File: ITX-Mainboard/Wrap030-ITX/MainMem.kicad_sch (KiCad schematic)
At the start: 28 parts, among them U2 TE-822021-4, U4 74HC245, U5 74HC245, U6 74HC245, U7 74HC245, U8 TE-822021-4

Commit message: Schematic substantial completion
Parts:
- C1: footprint Capacitor_SMD:C_0805_2012Metric -> Capacitor_SMD:C_0402_1005Metric_Pad0.74x0.62mm_HandSolder; JLC-Part (none) -> https://jlcpcb.com/partdetail/1877-CL05B104KO5NNNC/C1525
- C15: footprint Capacitor_SMD:C_0805_2012Metric -> Capacitor_SMD:C_0402_1005Metric_Pad0.74x0.62mm_HandSolder; JLC-Part (none) -> https://jlcpcb.com/partdetail/53938-CL05A105KA5NQNC/C52923
- RN1: Mouser-Part (none) -> 603-YC124-JR-1033RL; Notes (none) -> 33R x4
- U4, U5, U6, U7: footprint (none) -> Package_DIP:DIP-20_W7.62mm_Socket

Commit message: PCB substantial completion
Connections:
- net FC0 is gone; now on net MEM-A0: VGEN1.12 (IO3)
- net FC1 is gone; now on net CPU-A2: VGEN1.11 (IO5)
- net FC2 is gone; now on net CPU-A3: VGEN1.10 (IO6)
- net CPU-A0: now also VGEN1.51 (IO77); no longer VGEN1.44 (IO65)
- net CPU-A1: now also VGEN1.54 (IO83); no longer VGEN1.45 (IO67)
- net CPU-A10: now also VGEN1.79 (IO125); no longer VGEN1.56 (IO86)
- net CPU-A11: now also VGEN1.77 (IO123); no longer VGEN1.57 (IO88)
- net CPU-A12: now also VGEN1.75 (IO118); no longer VGEN1.58 (IO91)
- net CPU-A13: now also VGEN1.76 (IO120); no longer VGEN1.60 (IO93)
- net CPU-A14: now also VGEN1.74 (IO117); no longer VGEN1.61 (IO94)
- net CPU-A15: now also VGEN1.73 (IO115); no longer VGEN1.63 (IO97)
- net CPU-A16: now also VGEN1.69 (IO107); no longer VGEN1.64 (IO99)
- net CPU-A17: now also VGEN1.70 (IO109); no longer VGEN1.65 (IO101)
- net CPU-A2: no longer VGEN1.46 (IO69)
- net CPU-A20: now also VGEN1.64 (IO99); no longer VGEN1.69 (IO107)
- net CPU-A21: now also VGEN1.65 (IO101); no longer VGEN1.70 (IO109)
- net CPU-A22: now also VGEN1.63 (IO97); no longer VGEN1.73 (IO115)
- net CPU-A23: now also VGEN1.60 (IO93); no longer VGEN1.74 (IO117)
- net CPU-A24: now also VGEN1.58 (IO91); no longer VGEN1.75 (IO118)
- net CPU-A25: now also VGEN1.61 (IO94); no longer VGEN1.76 (IO120)
- net CPU-A26: now also VGEN1.57 (IO88); no longer VGEN1.77 (IO123)
- net CPU-A27: now also VGEN1.56 (IO86); no longer VGEN1.79 (IO125)
- net CPU-A28: now also VGEN1.52 (IO80); no longer VGEN1.80 (IO126)
- net CPU-A29: now also VGEN1.55 (IO85); no longer VGEN1.81 (IO128)
- net CPU-A3: no longer VGEN1.48 (IO72)
- net CPU-A4: now also VGEN1.8 (IO11); no longer VGEN1.49 (IO73)
- net CPU-A5: now also VGEN1.6 (IO13); no longer VGEN1.50 (IO75)
- net CPU-A6: now also VGEN1.9 (IO8); no longer VGEN1.51 (IO77)
- net CPU-A7: now also VGEN1.4 (IO16); no longer VGEN1.52 (IO80)
- net CPU-A8: now also VGEN1.80 (IO126); no longer VGEN1.54 (IO83)
- net CPU-A9: now also VGEN1.5 (IO14); no longer VGEN1.55 (IO85)
- net CPU-D0: now also U7.11 (B7); no longer U4.18 (B0)
- net CPU-D1: now also U7.12 (B6); no longer U4.17 (B1)
- net CPU-D10: now also U5.13 (B5); no longer U5.16 (B2)
- net CPU-D11: now also U5.14 (B4); no longer U5.15 (B3)
- net CPU-D12: now also U5.15 (B3); no longer U5.14 (B4)
- net CPU-D13: now also U5.16 (B2); no longer U5.13 (B5)
- net CPU-D14: now also U5.17 (B1); no longer U5.12 (B6)
- net CPU-D15: now also U5.18 (B0); no longer U5.11 (B7)
- net CPU-D16: now also U4.11 (B7); no longer U6.18 (B0)
- net CPU-D17: now also U4.12 (B6); no longer U6.17 (B1)
- net CPU-D18: now also U4.13 (B5); no longer U6.16 (B2)
- net CPU-D19: now also U4.14 (B4); no longer U6.15 (B3)
- net CPU-D2: now also U7.13 (B5); no longer U4.16 (B2)
- net CPU-D20: now also U4.15 (B3); no longer U6.14 (B4)
- net CPU-D21: now also U4.16 (B2); no longer U6.13 (B5)
- net CPU-D22: now also U4.17 (B1); no longer U6.12 (B6)
- net CPU-D23: now also U4.18 (B0); no longer U6.11 (B7)
- net CPU-D24: now also U6.11 (B7); no longer U7.18 (B0)
- net CPU-D25: now also U6.12 (B6); no longer U7.17 (B1)
- net CPU-D26: now also U6.13 (B5); no longer U7.16 (B2)
- net CPU-D27: now also U6.14 (B4); no longer U7.15 (B3)
- net CPU-D28: now also U6.15 (B3); no longer U7.14 (B4)
- net CPU-D29: now also U6.16 (B2); no longer U7.13 (B5)
- net CPU-D3: now also U7.14 (B4); no longer U4.15 (B3)
- net CPU-D30: now also U6.17 (B1); no longer U7.12 (B6)
- net CPU-D31: now also U6.18 (B0); no longer U7.11 (B7)
- net CPU-D4: now also U7.15 (B3); no longer U4.14 (B4)
- net CPU-D5: now also U7.16 (B2); no longer U4.13 (B5)
- net CPU-D6: now also U7.17 (B1); no longer U4.12 (B6)
- net CPU-D7: now also U7.18 (B0); no longer U4.11 (B7)
- net CPU-D8: now also U5.11 (B7); no longer U5.18 (B0)
- net CPU-D9: now also U5.12 (B6); no longer U5.17 (B1)
- net MEM-A0: no longer VGEN1.4 (IO16)
- net MEM-A1: now also VGEN1.15 (IO29); no longer VGEN1.22 (IO17)
- net MEM-A10: now also RN1.4 (R4.1), VGEN1.22 (IO17); no longer RN1.3 (R3.1), VGEN1.29 (IO38)
- net MEM-A10R: now also RN1.5 (R4.2); no longer RN1.6 (R3.2)
- net MEM-A11: now also RN1.2 (R2.1), VGEN1.25 (IO45); no longer RN1.4 (R4.1), VGEN1.28 (IO40)
- net MEM-A11R: now also RN1.7 (R2.2); no longer RN1.5 (R4.2)
- net MEM-A2: now also VGEN1.17 (IO25); no longer VGEN1.21 (IO19)
- net MEM-A3: now also VGEN1.16 (IO27); no longer VGEN1.20 (IO21)
- net MEM-A5: now also VGEN1.21 (IO19); no longer VGEN1.17 (IO25)
- net MEM-A6: now also VGEN1.20 (IO21); no longer VGEN1.16 (IO27)
- net MEM-A7: now also RN1.1 (R1.1), VGEN1.24 (IO46); no longer RN1.4 (R4.1), VGEN1.15 (IO29)
- net MEM-A7R: now also RN1.8 (R1.2); no longer RN1.5 (R4.2)
- net MEM-A8: now also RN1.3 (R3.1), VGEN1.27 (IO43); no longer RN1.1 (R1.1), VGEN1.31 (IO35)
- net MEM-A8R: now also RN1.6 (R3.2); no longer RN1.8 (R1.2)
- net MEM-A9: now also RN1.4 (R4.1), VGEN1.28 (IO40); no longer RN1.2 (R2.1), VGEN1.30 (IO37)
- net MEM-A9R: now also RN1.5 (R4.2); no longer RN1.7 (R2.2)
- net R/~{W}: now also VGEN1.81 (IO128); no longer VGEN1.5 (IO14)
- net SIZ0: now also VGEN1.48 (IO72); no longer VGEN1.9 (IO8)
- net SIZ1: now also VGEN1.49 (IO73); no longer VGEN1.8 (IO11)
- net ~{AS}: now also VGEN1.50 (IO75); no longer VGEN1.6 (IO13)
- net ~{MEM-CAS0}: now also RN1.3 (R3.1), VGEN1.35 (IO59); no longer RN1.1 (R1.1), VGEN1.40 (IO51)
- net ~{MEM-CAS1R}: now also RN1.5 (R4.2); no longer RN1.7 (R2.2)
- net ~{MEM-CAS1}: now also RN1.4 (R4.1), VGEN1.37 (IO56); no longer RN1.2 (R2.1), VGEN1.39 (IO53)
- net ~{MEM-CAS2R}: now also RN1.7 (R2.2); no longer RN1.6 (R3.2)
- net ~{MEM-CAS2}: now also RN1.1 (R1.1), VGEN1.33 (IO64); no longer RN1.3 (R3.1), VGEN1.37 (IO56)
- net ~{MEM-CAS3R}: now also RN1.6 (R3.2); no longer RN1.5 (R4.2)
- net ~{MEM-CAS3}: now also RN1.2 (R2.1); no longer RN1.4 (R4.1)
- net ~{MEM-RAS0R}: now also RN1.5 (R4.2); no longer RN1.8 (R1.2)
- net ~{MEM-RAS0}: now also RN1.4 (R4.1), VGEN1.34 (IO61); no longer RN1.1 (R1.1), VGEN1.27 (IO43)
- net ~{MEM-RAS1R}: now also RN1.6 (R3.2); no longer RN1.7 (R2.2)
- net ~{MEM-RAS1}: now also RN1.3 (R3.1), VGEN1.31 (IO35); no longer RN1.2 (R2.1), VGEN1.25 (IO45)
- net ~{MEM-RAS2R}: now also RN1.7 (R2.2); no longer RN1.6 (R3.2)
- net ~{MEM-RAS2}: now also RN1.2 (R2.1), VGEN1.30 (IO37); no longer RN1.3 (R3.1), VGEN1.24 (IO46)
- net ~{MEM-RAS3R}: now also RN1.8 (R1.2); no longer RN1.5 (R4.2)
- net ~{MEM-RAS3}: now also RN1.1 (R1.1), VGEN1.29 (IO38); no longer RN1.4 (R4.1), VGEN1.41 (IO49)
- net ~{MEM-WE}: now also VGEN1.40 (IO51); no longer VGEN1.35 (IO59)
- net ~{RAM-DSACK}: now also VGEN1.39 (IO53); no longer VGEN1.33 (IO64)

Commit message: Completing PCB Routing
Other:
- title: Wrap030 ITX -> Wrap030-ATX Mainboard
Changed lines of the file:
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@@
   (paper "USLetter")
   (title_block
-    (title "Wrap030 ITX")
-    (date "2023-03-15")
-    (rev "0")
+    (title "Wrap030-ATX Mainboard")
+    (date "2023-03-26")
+    (rev "1")
     (company "techav")
   )

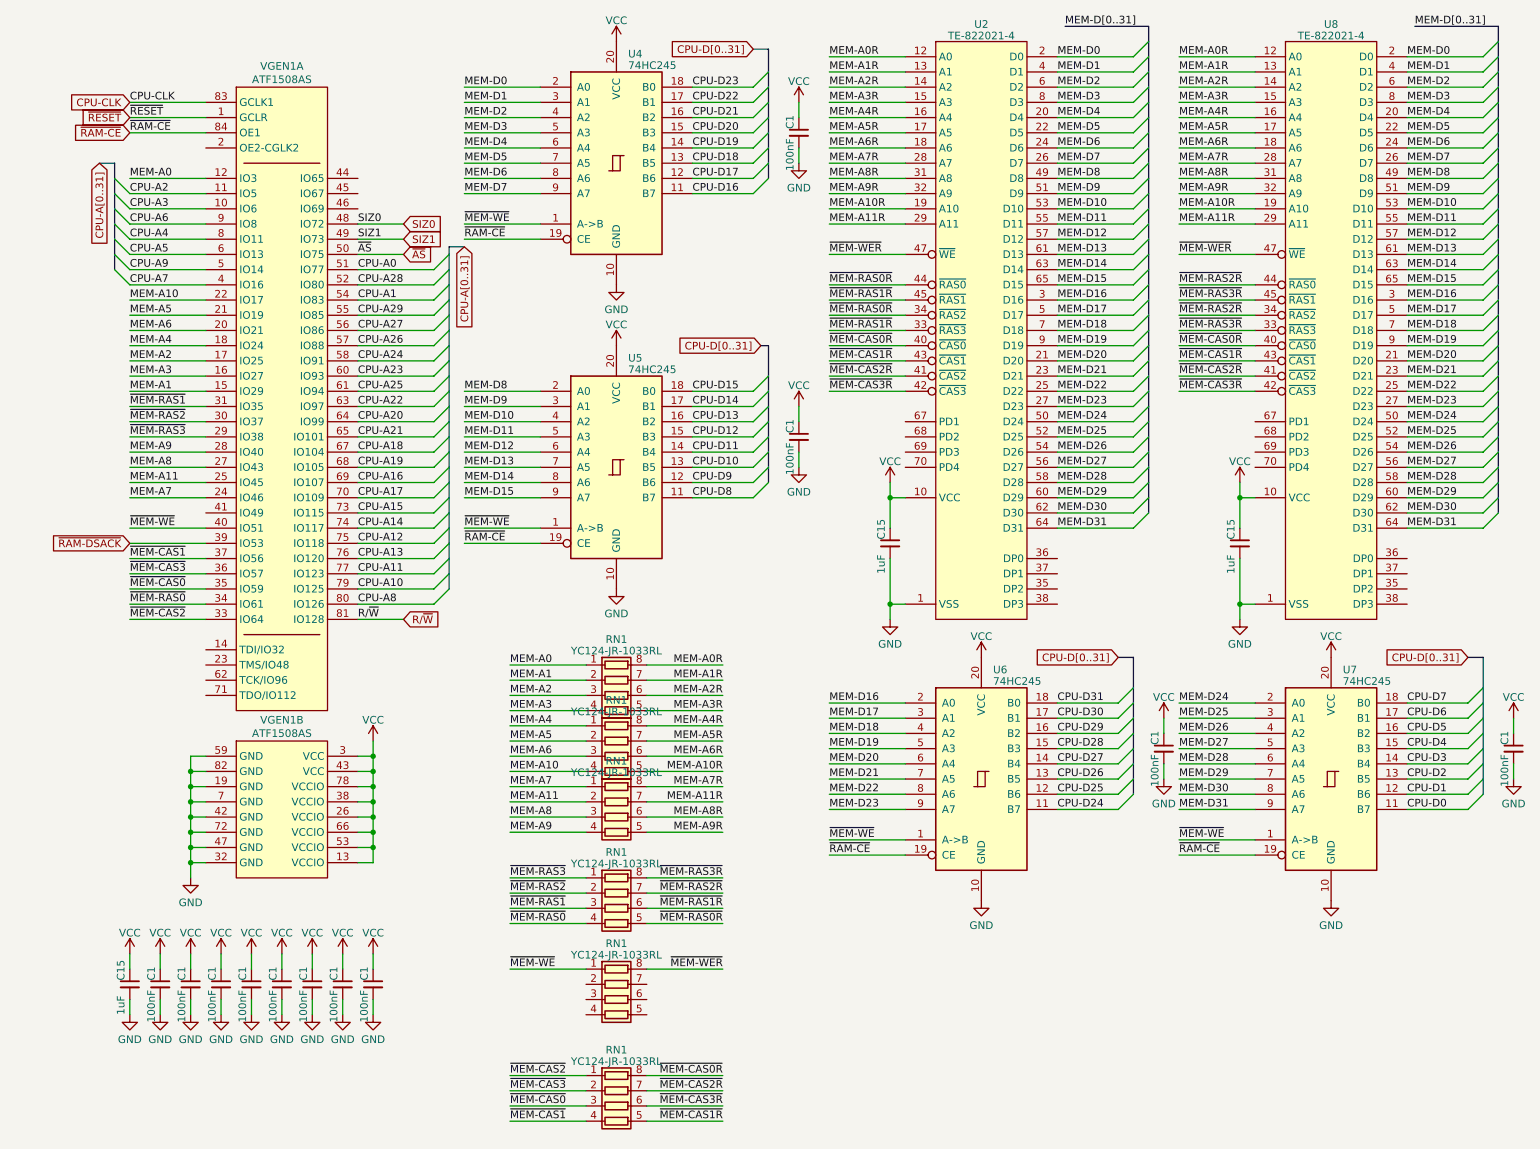
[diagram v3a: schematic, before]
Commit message: PCB Silkscreen & DRC Cleanup
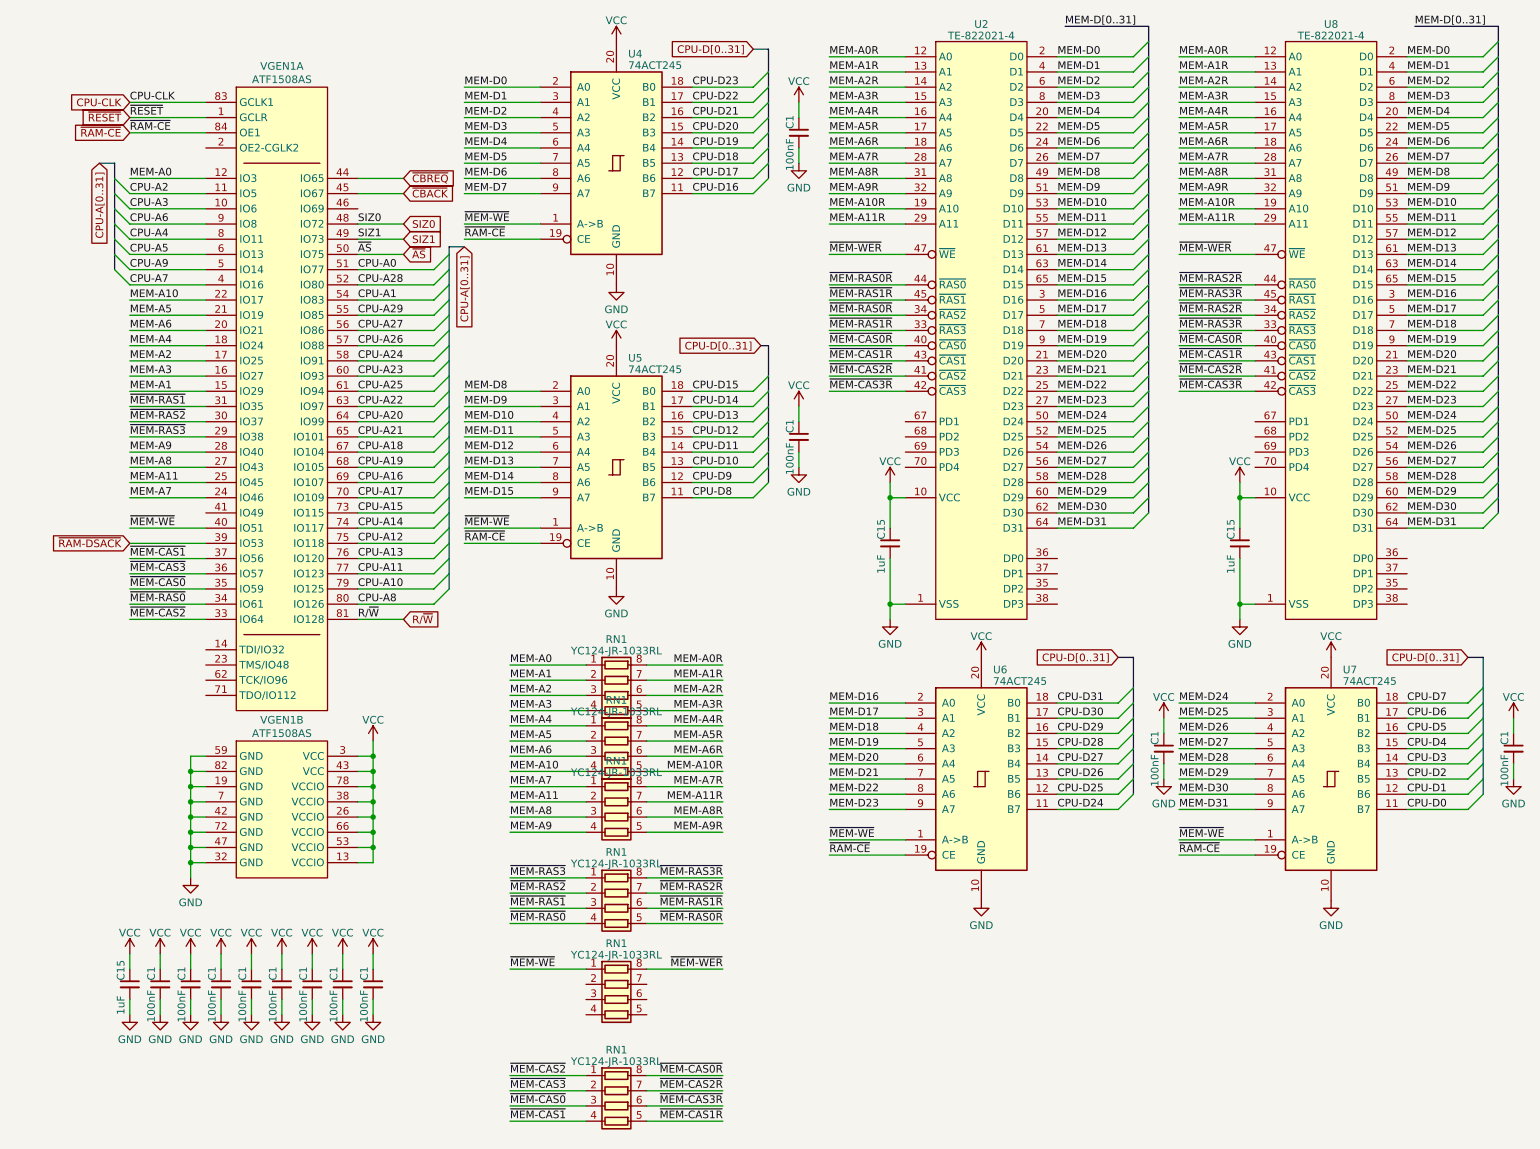
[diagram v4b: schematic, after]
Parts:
- U4, U5, U6, U7: value 74HC245 -> 74ACT245
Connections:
- net ~{CBREQ}: now reaches VGEN1.44 (IO65)
- net ~{CBACK}: now reaches VGEN1.45 (IO67)
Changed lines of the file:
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@@
     (stroke (width 0) (type default))
   )
+  (wire (pts (xy 71.12 43.18) (xy 63.5 43.18))
+    (stroke (width 0) (type default))
+  )
   (bus (pts (xy 195.58 17.78) (xy 195.58 20.32))
     (stroke (width 0) (type default))
@@
     (stroke (width 0) (type default))
   )
+  (wire (pts (xy 71.12 40.64) (xy 63.5 40.64))
+    (stroke (width 0) (type default))
+  )
   (wire (pts (xy 200.66 48.26) (xy 213.36 48.26))
     (stroke (width 0) (type default))
@@
     )
   )
+  (global_label "~{CBREQ}" (shape input) (at 71.12 40.64 0) (fields_autoplaced)
+    (effects (font (size 1.27 1.27)) (justify left))
+    (property "Intersheetrefs" "${INTERSHEET_REFS}" (at 80.3153 40.64 0)
+      (effects (font (size 1.27 1.27)) (justify left) hide)
+    )
+  )
   (global_label "SIZ1" (shape input) (at 71.12 50.8 0) (fields_autoplaced)
     (effects (font (size 1.27 1.27)) (justify left))
@@
     )
   )
+  (global_label "~{CBACK}" (shape input) (at 71.12 43.18 0) (fields_autoplaced)
+    (effects (font (size 1.27 1.27)) (justify left))
+    (property "Intersheetrefs" "${INTERSHEET_REFS}" (at 80.1944 43.18 0)
+      (effects (font (size 1.27 1.27)) (justify left) hide)
+    )
+  )
   (global_label "CPU-D[0..31]" (shape input) (at 130.81 68.58 180) (fields_autoplaced)
     (effects (font (size 1.27 1.27)) (justify right))
@@
       (effects (font (size 1.27 1.27)) (justify left))
     )
-    (property "Value" "74HC245" (at 108.6359 72.5711 0)
+    (property "Value" "74ACT245" (at 108.6359 72.5711 0)
       (effects (font (size 1.27 1.27)) (justify left))
     )
@@
       (effects (font (size 1.27 1.27)) (justify left))
     )
-    (property "Value" "74HC245" (at 228.0159 124.6411 0)
+    (property "Value" "74ACT245" (at 228.0159 124.6411 0)
       (effects (font (size 1.27 1.27)) (justify left))
     )
@@
       (effects (font (size 1.27 1.27)) (justify left))
     )
-    (property "Value" "74HC245" (at 169.5959 124.6411 0)
+    (property "Value" "74ACT245" (at 169.5959 124.6411 0)
       (effects (font (size 1.27 1.27)) (justify left))
     )
@@
       (effects (font (size 1.27 1.27)) (justify left))
     )
-    (property "Value" "74HC245" (at 108.6359 21.7711 0)
+    (property "Value" "74ACT245" (at 108.6359 21.7711 0)
       (effects (font (size 1.27 1.27)) (justify left))
     )

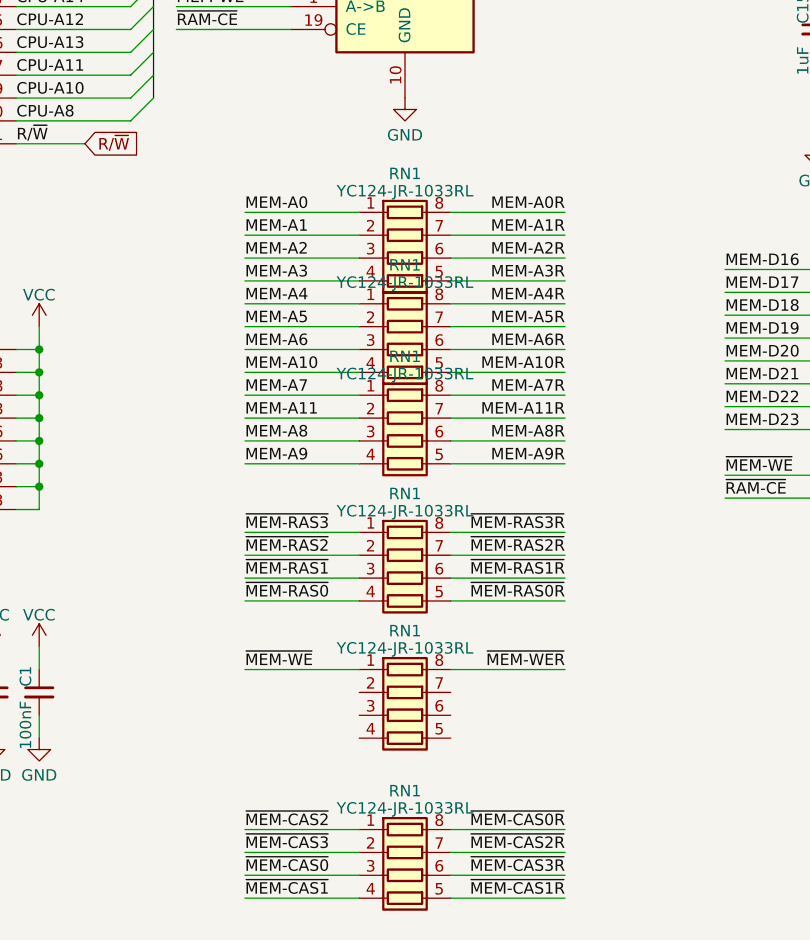
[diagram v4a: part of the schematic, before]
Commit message: Replace resistor nets with 0402 & update gerbers
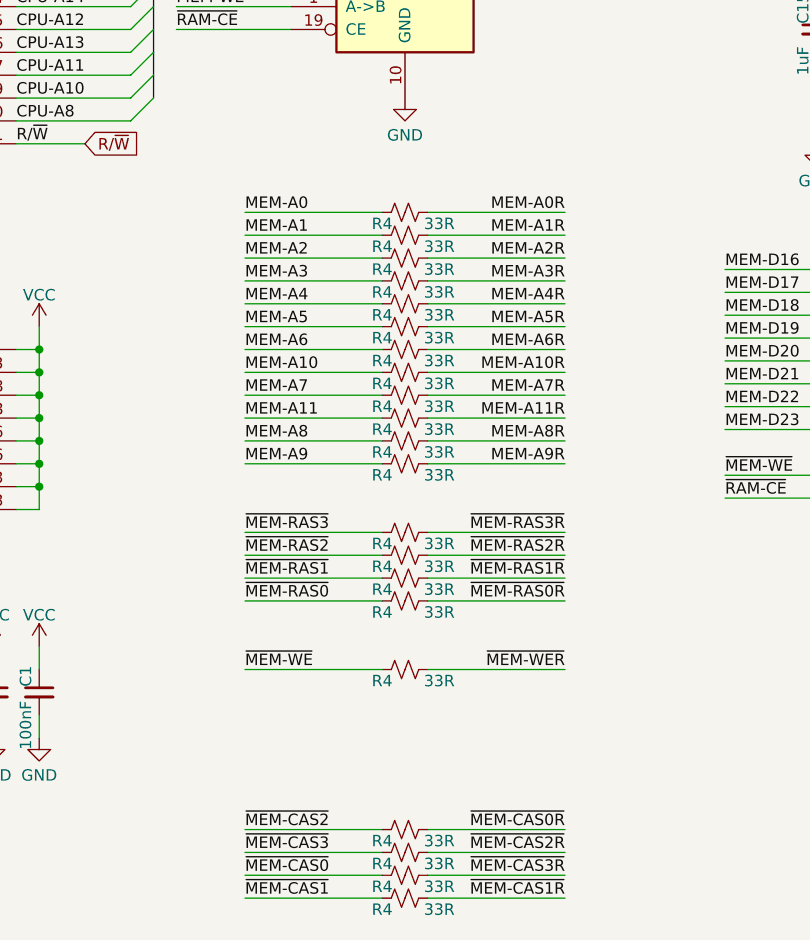
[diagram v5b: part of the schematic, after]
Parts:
- removed RN1 (x6): YC124-JR-1033RL, Resistor_SMD:R_Array_Convex_4x1206, symbol Device:R_Pack04
- added R4 (x21): 33R, Resistor_SMD:R_0603_1608Metric_Pad0.98x0.95mm_HandSolder, symbol Device:R_Small_US
- C1: Mouser-Part (none) -> 187-CL05B104KO5NNNC; Notes (none) -> JLC
- C15: Mouser-Part (none) -> 187-CL05A105KA5NQNC; Notes (none) -> JLC
- U2, U8: Mouser-Part (none) -> 571-5822021-4; Notes (none) -> OFE
- U4, U5, U6, U7: Mouser-Part (none) -> 595-SN74ACT245N; Notes (none) -> OFE; Socket-Mouser (none) -> 571-1-2199298-6
- VGEN1: Mouser-Part (none) -> 556-ATF1508AS-10JU84; Notes (none) -> OFE; Socket-Mouser (none) -> 575-948424
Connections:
- net MEM-A0: now also R4.1
- net MEM-A0R: now also R4.2
- net MEM-A1: now also R4.1
- net MEM-A10: now also R4.1
- net MEM-A10R: now also R4.2
- net MEM-A11: now also R4.1
- net MEM-A11R: now also R4.2
- net MEM-A1R: now also R4.2
- net MEM-A2: now also R4.1
- net MEM-A2R: now also R4.2
- net MEM-A3: now also R4.1
- net MEM-A3R: now also R4.2
- net MEM-A4: now also R4.1
- net MEM-A4R: now also R4.2
- net MEM-A5: now also R4.1
- net MEM-A5R: now also R4.2
- net MEM-A6: now also R4.1
- net MEM-A6R: now also R4.2
- net MEM-A7: now also R4.1
- net MEM-A7R: now also R4.2
- net MEM-A8: now also R4.1
- net MEM-A8R: now also R4.2
- net MEM-A9: now also R4.1
- net MEM-A9R: now also R4.2
- net ~{MEM-CAS0R}: now also R4.2
- net ~{MEM-CAS0}: now also R4.1
- net ~{MEM-CAS1R}: now also R4.2
- net ~{MEM-CAS1}: now also R4.1
- net ~{MEM-CAS2R}: now also R4.2
- net ~{MEM-CAS2}: now also R4.1
- net ~{MEM-CAS3R}: now also R4.2
- net ~{MEM-CAS3}: now also R4.1
- net ~{MEM-RAS0R}: now also R4.2
- net ~{MEM-RAS0}: now also R4.1
- net ~{MEM-RAS1R}: now also R4.2
- net ~{MEM-RAS1}: now also R4.1
- net ~{MEM-RAS2R}: now also R4.2
- net ~{MEM-RAS2}: now also R4.1
- net ~{MEM-RAS3R}: now also R4.2
- net ~{MEM-RAS3}: now also R4.1
- net ~{MEM-WER}: now also R4.2
- net ~{MEM-WE}: now also R4.1
